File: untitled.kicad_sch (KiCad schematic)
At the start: 1 part

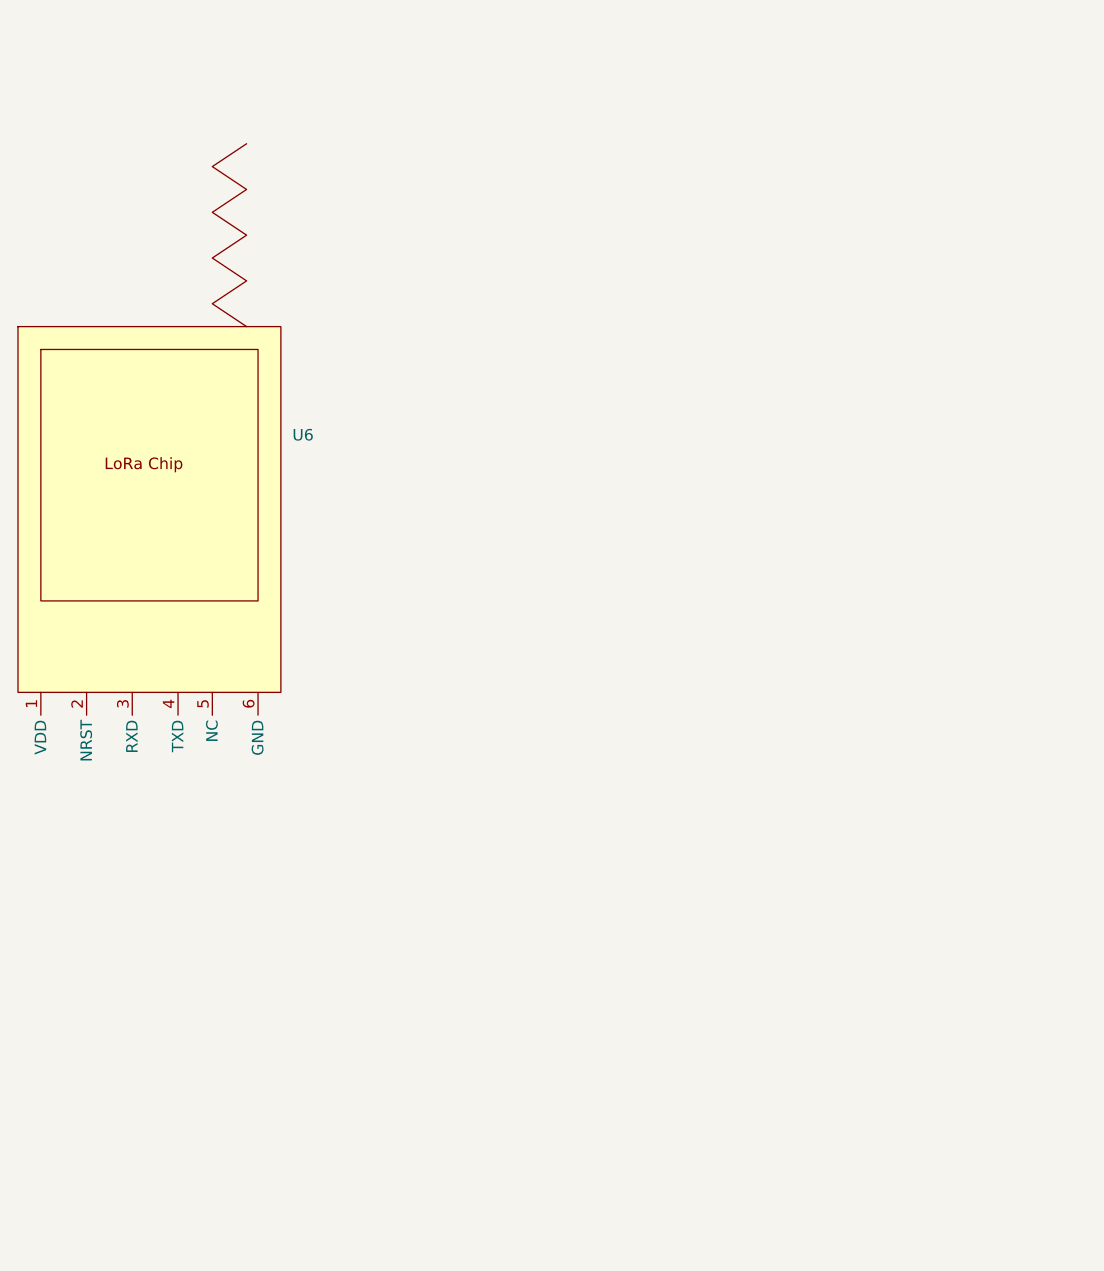
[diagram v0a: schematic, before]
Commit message: Updated the indivdual components.
Some of the individual components still need to be updated and completed. With the battery box, include the diode. The full schematic is not the update one as Andrew has the updated one with the correct flyback diode placement.
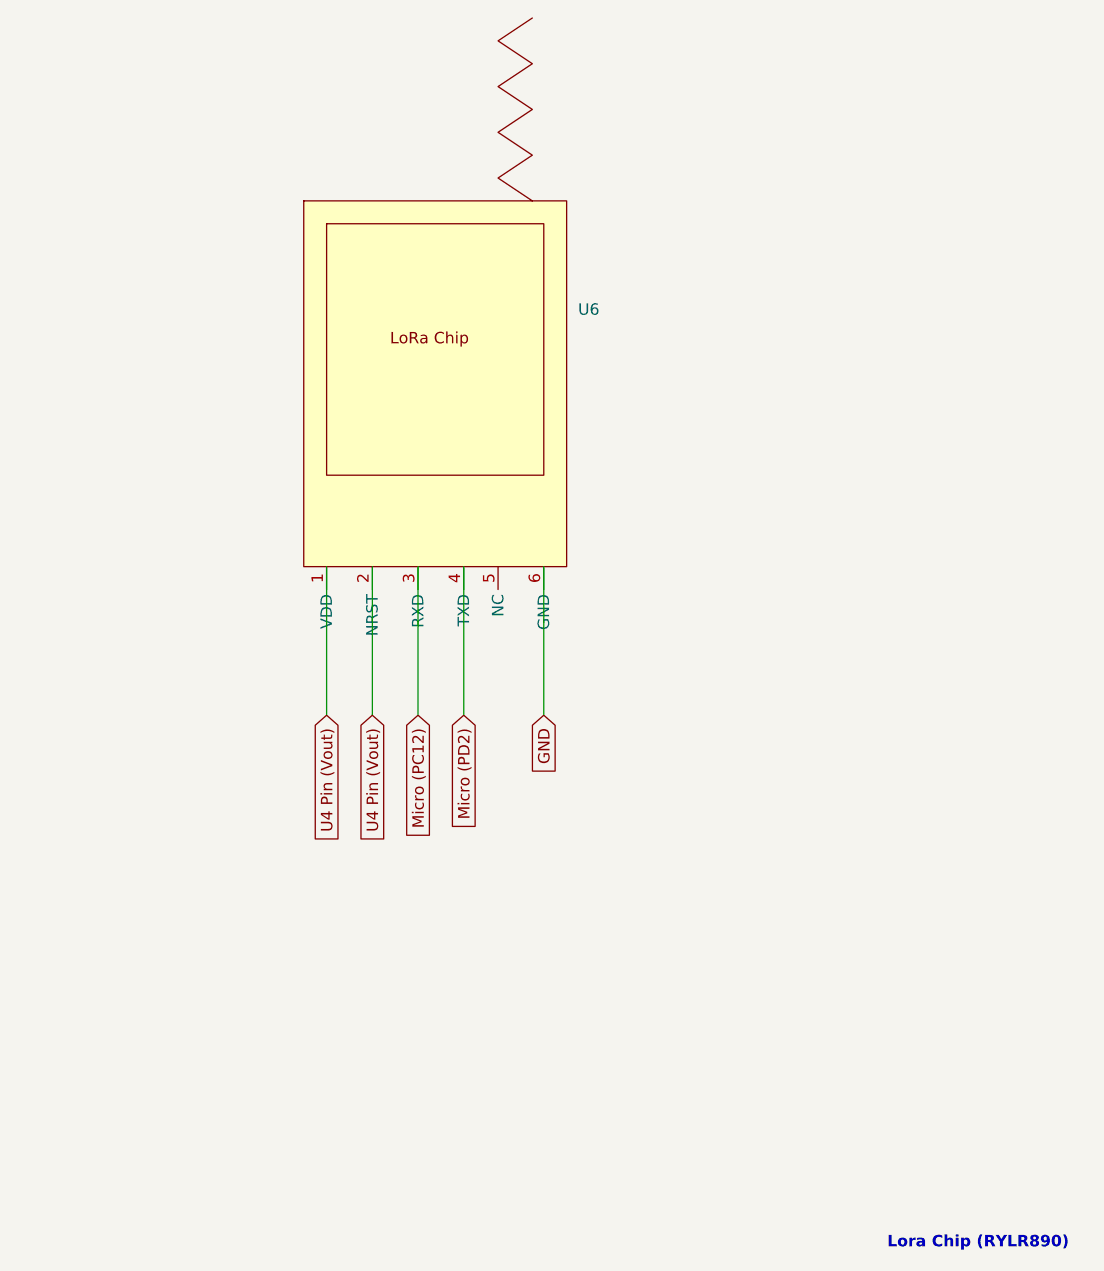
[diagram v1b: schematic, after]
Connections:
- net U4 Pin (Vout): now reaches U6.1 (VDD)
- net U4 Pin (Vout): now also U6.2 (NRST)
- net Micro (PC12): now reaches U6.3 (RXD)
- net Micro (PD2): now reaches U6.4 (TXD)
- net GND: now reaches U6.6 (GND)
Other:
- note added: "Lora Chip (RYLR890)"
- moved on the sheet: U6
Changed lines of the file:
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@@
 	(generator_version "8.0")
 	(paper "A4")
+	(wire
+		(pts
+			(xy 140.97 114.3) (xy 140.97 130.81)
+		)
+		(stroke
+			(width 0)
+			(type default)
+		)
+	)
+	(wire
+		(pts
+			(xy 135.89 114.3) (xy 135.89 130.81)
+		)
+		(stroke
+			(width 0)
+			(type default)
+		)
+	)
+	(wire
+		(pts
+			(xy 149.86 114.3) (xy 149.86 130.81)
+		)
+		(stroke
+			(width 0)
+			(type default)
+		)
+	)
+	(wire
+		(pts
+			(xy 130.81 114.3) (xy 130.81 130.81)
+		)
+		(stroke
+			(width 0)
+			(type default)
+		)
+	)
+	(wire
+		(pts
+			(xy 125.73 114.3) (xy 125.73 130.81)
+		)
+		(stroke
+			(width 0)
+			(type default)
+		)
+	)
+	(text "Lora Chip (RYLR890)"
+		(exclude_from_sim no)
+		(at 198.12 189.484 0)
+		(effects
+			(font
+				(size 1.27 1.27)
+				(thickness 0.254)
+				(bold yes)
+			)
+		)
+	)
+	(global_label "Micro (PD2)"
+		(shape input)
+		(at 140.97 130.81 270)
+		(fields_autoplaced yes)
+		(effects
+			(font
+				(size 1.27 1.27)
+			)
+			(justify right)
+		)
+		(property "Intersheetrefs" "${INTERSHEET_REFS}"
+			(at 140.97 145.2857 90)
+			(effects
+				(font
+					(size 1.27 1.27)
+				)
+				(justify right)
+				(hide yes)
+			)
+		)
+	)
+	(global_label "GND"
+		(shape input)
+		(at 149.86 130.81 270)
+		(fields_autoplaced yes)
+		(effects
+			(font
+				(size 1.27 1.27)
+			)
+			(justify right)
+		)
+		(property "Intersheetrefs" "${INTERSHEET_REFS}"
+			(at 149.86 137.6657 90)
+			(effects
+				(font
+					(size 1.27 1.27)
+				)
+				(justify right)
+				(hide yes)
+			)
+		)
+	)
+	(global_label "Micro (PC12)"
+		(shape input)
+		(at 135.89 130.81 270)
+		(fields_autoplaced yes)
+		(effects
+			(font
+				(size 1.27 1.27)
+			)
+			(justify right)
+		)
+		(property "Intersheetrefs" "${INTERSHEET_REFS}"
+			(at 135.89 146.4952 90)
+			(effects
+				(font
+					(size 1.27 1.27)
+				)
+				(justify right)
+				(hide yes)
+			)
+		)
+	)
+	(global_label "U4 Pin (Vout)"
+		(shape input)
+		(at 130.81 130.81 270)
+		(fields_autoplaced yes)
+		(effects
+			(font
+				(size 1.27 1.27)
+			)
+			(justify right)
+		)
+		(property "Intersheetrefs" "${INTERSHEET_REFS}"
+			(at 130.81 147.0999 90)
+			(effects
+				(font
+					(size 1.27 1.27)
+				)
+				(justify right)
+				(hide yes)
+			)
+		)
+	)
+	(global_label "U4 Pin (Vout)"
+		(shape input)
+		(at 125.73 130.81 270)
+		(fields_autoplaced yes)
+		(effects
+			(font
+				(size 1.27 1.27)
+			)
+			(justify right)
+		)
+		(property "Intersheetrefs" "${INTERSHEET_REFS}"
+			(at 125.73 147.0999 90)
+			(effects
+				(font
+					(size 1.27 1.27)
+				)
+				(justify right)
+				(hide yes)
+			)
+		)
+	)
 	(symbol
 		(lib_id "LoRa Chip:RYLR896")
-		(at 105.41 115.57 0)
+		(at 137.16 101.6 0)
 		(unit 1)
 		(exclude_from_sim no)
@@
 		(fields_autoplaced yes)
 		(property "Reference" "U6"
-			(at 121.92 99.695 0)
+			(at 153.67 85.725 0)
 			(effects
 				(font
@@
 		)
 		(property "Value" "~"
-			(at 105.41 115.57 0)
+			(at 137.16 101.6 0)
 			(effects
 				(font
@@
 		)
 		(property "Footprint" "LoRa Chip:LoRa Chip"
-			(at 105.41 115.57 0)
+			(at 137.16 101.6 0)
 			(effects
 				(font
@@
 		)
 		(property "Datasheet" ""
-			(at 105.41 115.57 0)
+			(at 137.16 101.6 0)
 			(effects
 				(font
@@
 		)
 		(property "Description" ""
-			(at 105.41 115.57 0)
-			(effects
-				(font
+			(at 137.16 101.6 0)
+			(effects
+				(font
